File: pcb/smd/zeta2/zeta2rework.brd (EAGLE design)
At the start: 101.3 x 85.1 mm, 38 parts, among them IC1 MAX6520, IC2 L293DD, U2 INA219, U4 INA219

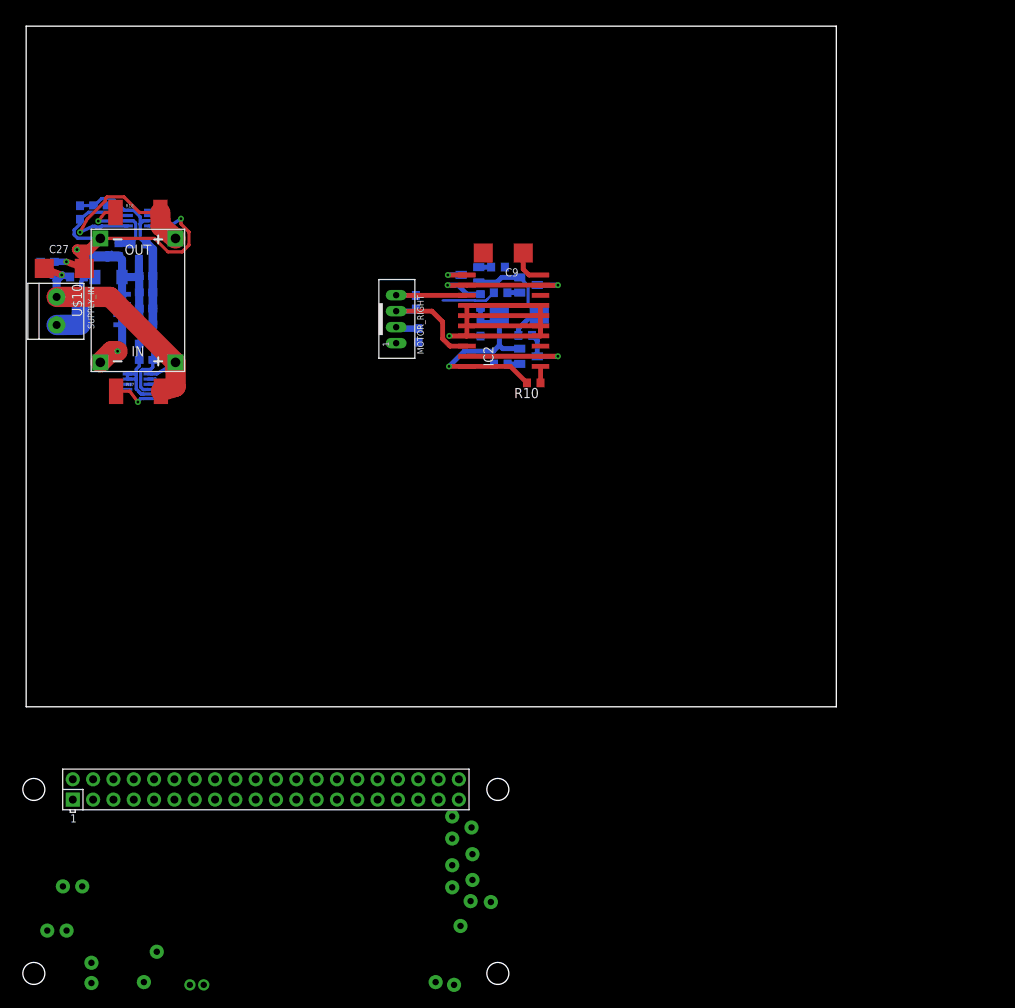
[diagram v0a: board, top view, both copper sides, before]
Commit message: added i2c device
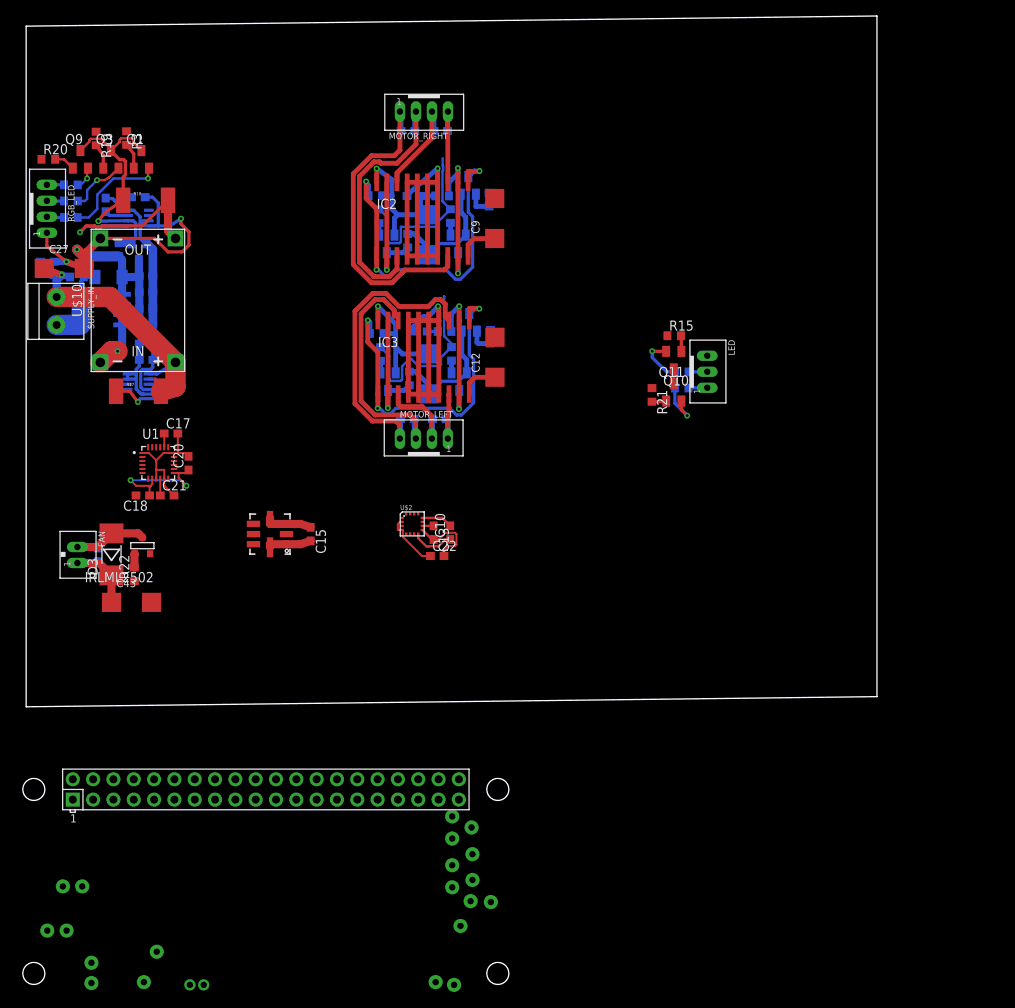
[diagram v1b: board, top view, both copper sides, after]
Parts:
- added C10: 0.22µF, rcl:C0603
- added C12, C43: 47µF, rcl:SMC_C
- added C13, C22: 4.7µF, rcl:C0603
- added C14: 100µF, rcl:SMC_C
- added C15: 100nF, rcl:C0603
- added C17: 2,2nF, rcl:C0603
- added C18, C20, C21: 0.1µF, rcl:C0603
- added C2: 0.1nF, rcl:C0603
- added C3, C31, C41: 10nF, rcl:C0603
- added D3: 1N4004 SMD, diode:MELF-MLL41
- added FAN: JST-PH_2-PIN_HEADER, srg:JST_B2B-PH_HEADER
- added IC3: L293DD, st-microelectronics:SO20
- added IRLML2502: (no value), zetex:SOT-23
- added LED: JST-PH_3-PIN_HEADER, srg:JST_B3B-PH_HEADER
- added MOTOR_LEFT, RGB_LED: JST-PH_4-PIN_HEADER, srg:JST_B4B-PH_HEADER
- added Q1, Q10, Q11, Q3, Q5, Q6, Q8, Q9: (no value), semicon-smd-ipc:SOT23
- added R12, R14, R8: 100k, rcl:R0603
- added R13, R5, R6: 500R, rcl:R0603
- added R15, R19, R20, R21, R3: 500, rcl:R0603
- added R16, R26, R27, R28, R4: 220R, rcl:R0603
- added R22: 22R, rcl:R0603
- added U$2: HMC5883L, HMC5883L:LPCC-16
- added U$3: BMP085, BMP085:BMP085
- added U1: MPU-6050, MPU-6050:QFN50P400X400X95-24N
- moved R10 30.7 mm to (43.6, 60.1), flipped to the bottom
- moved MOTOR_RIGHT 26.2 mm to (49.7, 70.6), turned to 180 degrees
- moved C28 25.6 mm to (47.7, 68.1), turned to 0 degrees
- moved R1 23.9 mm to (44.1, 57.5), turned to 270 degrees
- moved Q2 22.6 mm to (45.1, 54.1), turned to 180 degrees
- moved C29 21.6 mm to (51.8, 68.2), turned to 0 degrees
- moved R7 18.9 mm to (47.7, 54.5), turned to 270 degrees
- moved C1 18.6 mm to (48.5, 60.0), turned to 0 degrees
- moved IC2 16.3 mm to (49.5, 57.1), turned to 0 degrees
- moved C11 15.5 mm to (50.0, 55.2), turned to 270 degrees
- moved R9 14.0 mm to (52.0, 60.0), turned to 0 degrees
- moved R11 11.4 mm to (53.0, 57.5), turned to 270 degrees
- moved Q4 11.2 mm to (55.3, 61.4), turned to 0 degrees
- moved Q7 10.2 mm to (54.0, 54.1), turned to 180 degrees
- moved R2 8.51 mm to (57.9, 59.6), turned to 270 degrees
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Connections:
- new net BMP_EOC: U$3.2
- new net HMC_RDY: U$2.15
- new net MPU_INT: U1.12
- new net M_DIR_2: R13.1, R5.1
- new net N$13: Q5.1, R5.2
- new net N$14: Q6.1, R6.2
- new net N$15: Q8.1, R13.2
- new net N$16: R27.2, RGB_LED.P3
- new net N$19: R28.2, RGB_LED.P2
- new net N$2: C31.2, IC3.18, MOTOR_LEFT.P3
- new net N$22: Q1.1, R3.2
- new net N$23: Q3.1, R19.2
- new net N$24: Q1.2, R28.1
- new net N$25: C3.2, IC3.8, MOTOR_LEFT.P1
- new net N$26: C3.1, IC3.3, MOTOR_LEFT.P2
- new net N$27: Q10.1, R15.2
- new net N$28: Q3.2, R27.1
- new net N$29: Q9.2, R26.1
- new net N$3: C31.1, IC3.13, MOTOR_LEFT.P4
- new net N$30: Q10.2, R4.1
- new net N$31: Q11.1, R21.2
- new net N$32: Q9.1, R20.2
- new net N$33: Q11.2, R16.1
- new net N$34: C17.1, U1.20
- new net N$35: LED.P1, R16.2
- new net N$36: C21.1, U1.10
- new net N$37: IRLML2502.3, R22.2
- new net N$38: C10.2, U$2.12
- new net N$39: C10.1, U$2.8
- new net N$4: R26.2, RGB_LED.P4
- new net N$40: C13.1, U$2.10
- new net N$48: LED.P2, R4.2
- new net N$55: C41.2, D3.A, FAN.P2, IRLML2502.1
- new net N$6: IC3.12, IC3.9, Q8.3, R8.1
- new net N$7: IC3.19, IC3.2, Q5.3, R14.2
- new net N$9: IC3.1, IC3.11, Q6.3, R12.1
- new net PWM_FAN: R22.1
- new net PWM_M_EN_2: R6.1
- new net SCL1: U$2.1
- new net SDA1: U$2.16
- net +3V3: now also C15.1, C18.1, C20.1, C22.1, U$2.13, U$2.2, U$2.4, U$3.3, U$3.4, U1.13, U1.8
- net +5V: now also C14.+, C2.1, IC3.20, Q1.3, Q10.3, Q11.3, Q3.3, Q5.2, Q9.3, R12.2, R8.2
- net +8V: now also C12.+, C41.1, C43.+, D3.C, FAN.P1, IC3.10
- net GND: now also C12.-, C13.2, C14.-, C15.2, C17.2, C18.2, C2.2, C20.2, C21.2, C22.2, C43.-, IC3.14, IC3.15, IC3.16, IC3.17, IC3.4, IC3.5, IC3.6, IC3.7, IRLML2502.2, LED.P3, Q6.2, Q8.2, R14.1, RGB_LED.P1, U$2.11, U$2.9, U$3.1, U$3.8, U1.1, U1.11, U1.18, U1.9
- net SCL: now also U$3.6, U1.23
- net SDA: now also U$3.7, U1.24
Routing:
- net GND: track 153.1 -> 254.5 mm, vias 5 -> 6
- net N$9: track 0.00 -> 42.5 mm, vias 0 -> 3
- net N$3: track 0.00 -> 38.2 mm
- net N$20: track 2.62 -> 40.7 mm
- net N$8: track 6.10 -> 43.2 mm, vias 1 -> 3
- net N$21: track 0.17 -> 33.7 mm
- net +5V: track 40.3 -> 72.4 mm, vias 2 -> 3
- net N$2: track 0.00 -> 29.8 mm
- net +3V3: track 34.5 -> 62.6 mm, vias 0 -> 2
- net M_DIR_2: track 0.00 -> 23.0 mm
- net N$6: track 0.00 -> 18.7 mm, vias 0 -> 2
- net +8V: track 14.1 -> 30.6 mm
- net N$7: track 0.00 -> 16.1 mm, vias 0 -> 1
- net M_DIR_1: track 6.82 -> 22.4 mm
- net N$24: track 0.00 -> 13.2 mm, vias 0 -> 1
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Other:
- board size 101.3 x 85.1 mm -> 106.3 x 86.4 mm

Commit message: worked on pcb, fixed stm32 layout
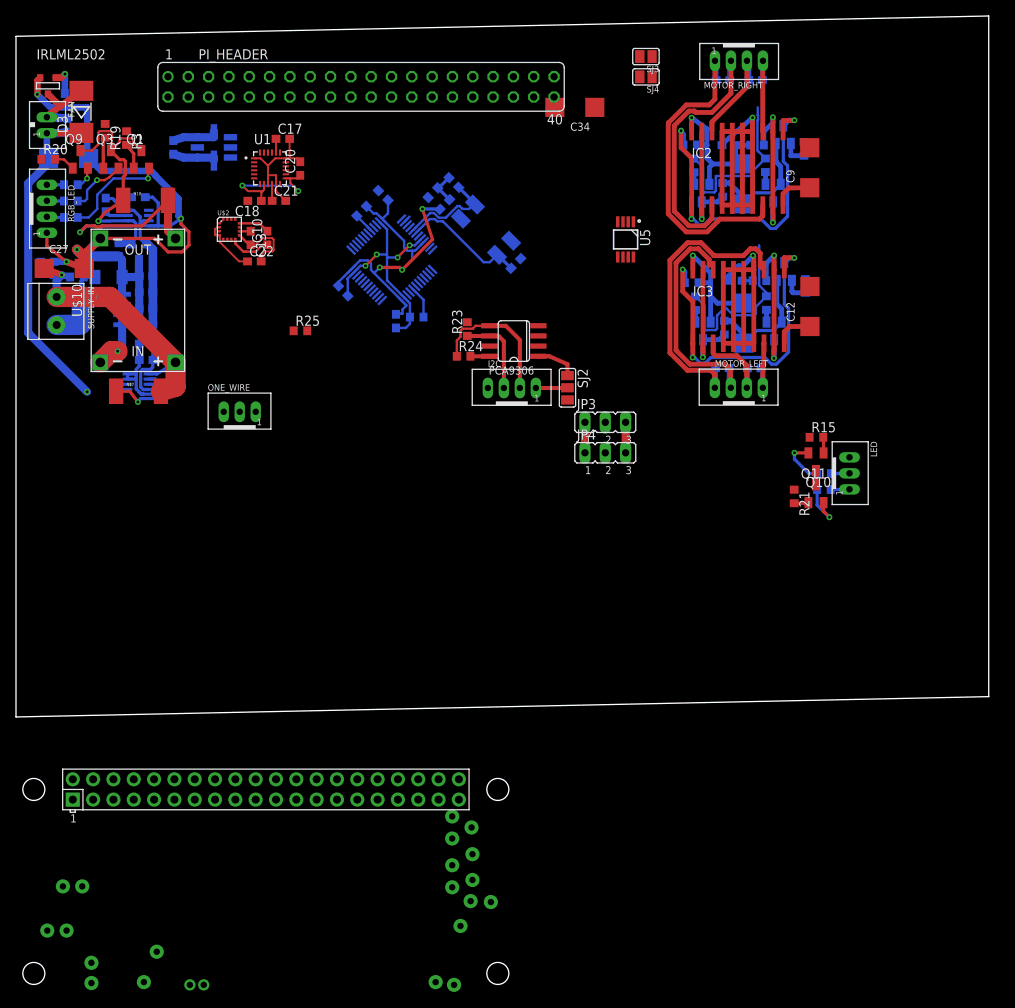
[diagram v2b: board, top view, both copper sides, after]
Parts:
- added C33, C38, C39, C40: 10nF, rcl:C0603
- added C34: 47µF, rcl:SMC_C
- added C36, C37: 10µF, rcl:C0603
- added I2C: JST-PH_4-PIN_HEADER, srg:JST_B4B-PH_HEADER
- added JP3, JP4: (no value), jumper:JP2
- added ONE_WIRE: JST-PH_3-PIN_HEADER, srg:JST_B3B-PH_HEADER
- added PCA9306: (no value), srg:SOIC-8
- added PI_HEADER: (no value), con-lsta:FE20-2
- added Q12: 8MHz, crystal-geyer_V1_0:7.0X5.0
- added R23, R24: 5k, rcl:R0603
- added R25: 4k7, rcl:R0603
- added R30, R31, R33: 100k, rcl:R0603
- added SJ2: (no value), jumper:SJ_2
- added SJ3, SJ4: (no value), microbuilder:SOLDERJUMPER_REFLOW_NOPASTE
- added U$4: STM32F103C8T6, STM32F103C8T6:LQFP48_7X7MM_0.5MMPP
- added U5: DS18B20U+, DS18B20U_:SOP65P490X95-8N
- moved R22 60.6 mm to (5.69, 72.8), flipped to the bottom, turned to 0 degrees
- moved IRLML2502 58.7 mm to (2.69, 73.8), turned to 0 degrees
- moved C43 56.1 mm to (5.31, 64.7), flipped to the bottom, turned to 180 degrees
- moved D3 55.4 mm to (6.91, 70.6)
- moved FAN 53.9 mm to (2.54, 69.0)
- moved C41 53.8 mm to (5.16, 68.9)
- moved C15 51.3 mm to (18.4, 66.1), flipped to the bottom
- moved U$3 48.8 mm to (23.5, 66.1), flipped to the bottom
- moved C10 43.3 mm to (30.1, 54.8)
- moved C13 43.3 mm to (28.1, 54.8)
- moved C22 43.3 mm to (28.5, 51.9)
- moved U$2 43.3 mm to (25.4, 55.9)
- moved C29 39.9 mm to (91.2, 74.5)
- moved R10 39.9 mm to (83.0, 66.4)
- moved C1 39.9 mm to (87.8, 66.4)
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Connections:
- new net ANALOG_3V3: U$4.10
- new net BOOT0: JP3.2, R31.2, U$4.44
- new net BOOT1: JP4.2, R33.1, U$4.20
- new net BOOT2: PI_HEADER.29
- new net BOOT3: PI_HEADER.27
- new net N$41: I2C.P1, PCA9306.7, PCA9306.8, R23.2, R24.2, SJ2.2
- new net N$42: I2C.P3, PCA9306.6, R23.1
- new net N$43: I2C.P2, PCA9306.5, R24.1
- new net N$44: PI_HEADER.37, SJ3.2
- new net N$45: PI_HEADER.35, SJ4.2
- new net N$46: C36.2, Q12.1, U$4.6
- new net N$47: C37.2, Q12.3, U$4.5
- new net N$49: R30.1, U$4.2
- new net NRST: PI_HEADER.26, U$4.7
- new net PIN_OUT: U$4.28
- new net SCL2: PCA9306.2
- new net SCL3: SJ4.1
- new net SDA2: PCA9306.3
- new net SDA3: SJ3.1
- new net SWCLK: PI_HEADER.20
- new net SWDCLK: U$4.37
- new net SWDIO: PI_HEADER.24, U$4.34
- new net S_DIR: U$4.14
- new net S_PWM_SPEED: U$4.19
- new net TEMPERATURE: ONE_WIRE.P2, R25.1, U5.1
- new net USART1_RX: U$4.31
- new net USART1_TX: U$4.30
- new net USART2_RX: PI_HEADER.34, U$4.13
- new net USART2_TX: PI_HEADER.32, U$4.12
- new net USB_DM: U$4.32
- new net USB_DP: U$4.33
- net +3V3: now also C33.1, C38.1, C39.1, C40.1, JP3.1, JP4.1, ONE_WIRE.P1, PCA9306.1, R25.2, R31.1, SJ2.1, U$4.24, U$4.36, U$4.48, U$4.9, U5.8
- net +5V: now also C34.+, PI_HEADER.38, PI_HEADER.40, SJ2.3
- net GND: now also C33.2, C34.-, C36.1, C37.1, C38.2, C39.2, C40.2, I2C.P4, JP3.3, JP4.3, ONE_WIRE.P3, PCA9306.4, PI_HEADER.1, PI_HEADER.12, PI_HEADER.15, PI_HEADER.22, PI_HEADER.28, PI_HEADER.31, PI_HEADER.36, PI_HEADER.8, R30.2, R33.2, U$4.23, U$4.35, U$4.47, U$4.8, U5.4
- net M_DIR_1: now also U$4.15, U$4.17
- net PWM_M_EN_1: now also U$4.16
- net PWM_M_EN_2: now also U$4.18
- net SCL: now also U$4.42
- net SDA: now also U$4.43
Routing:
- net GND: track 254.5 -> 323.8 mm, vias 6 -> 11
- net +3V3: track 62.6 -> 118.9 mm, vias 2 -> 5
- net +8V: track 30.6 -> 63.1 mm, vias 1 -> 2
- net N$43: track 0.00 -> 17.8 mm
- net N$46: track 0.00 -> 16.0 mm
- net N$47: track 0.00 -> 12.1 mm
- net N$42: track 0.00 -> 10.7 mm
- net N$41: track 0.00 -> 6.32 mm
- net BOOT1: track 0.00 -> 4.04 mm
- net +5V: track 72.4 -> 75.2 mm
- net BOOT0: track 0.00 -> 2.53 mm
- net N$37: track 1.73 -> 3.80 mm, vias 0 -> 1
- net N$55: track 11.7 -> 10.3 mm
- net N$49: track 0.00 -> 0.92 mm
- net N$23: track 3.16 -> 3.93 mm
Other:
- board size 106.3 x 86.4 mm -> 121.6 x 87.6 mm

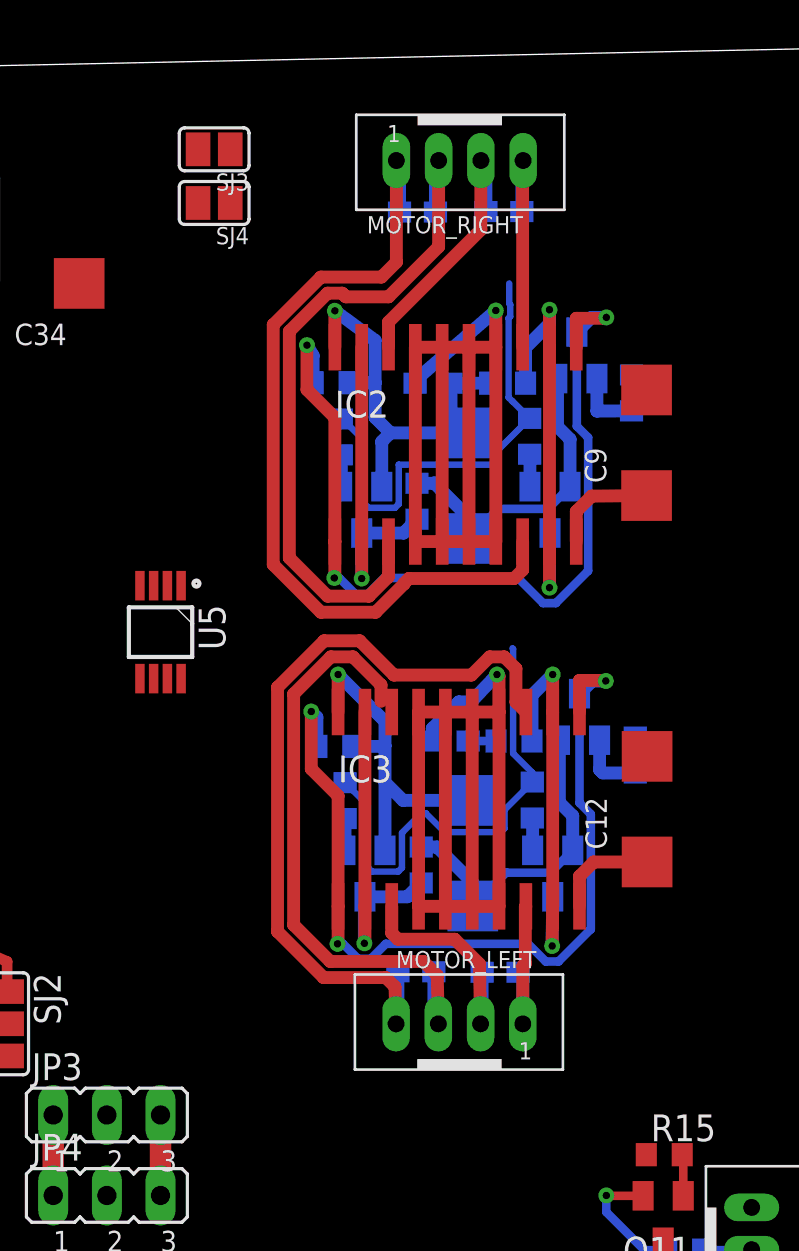
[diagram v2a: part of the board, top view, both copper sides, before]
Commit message: added temperature sensor to l239d, heatplate missing
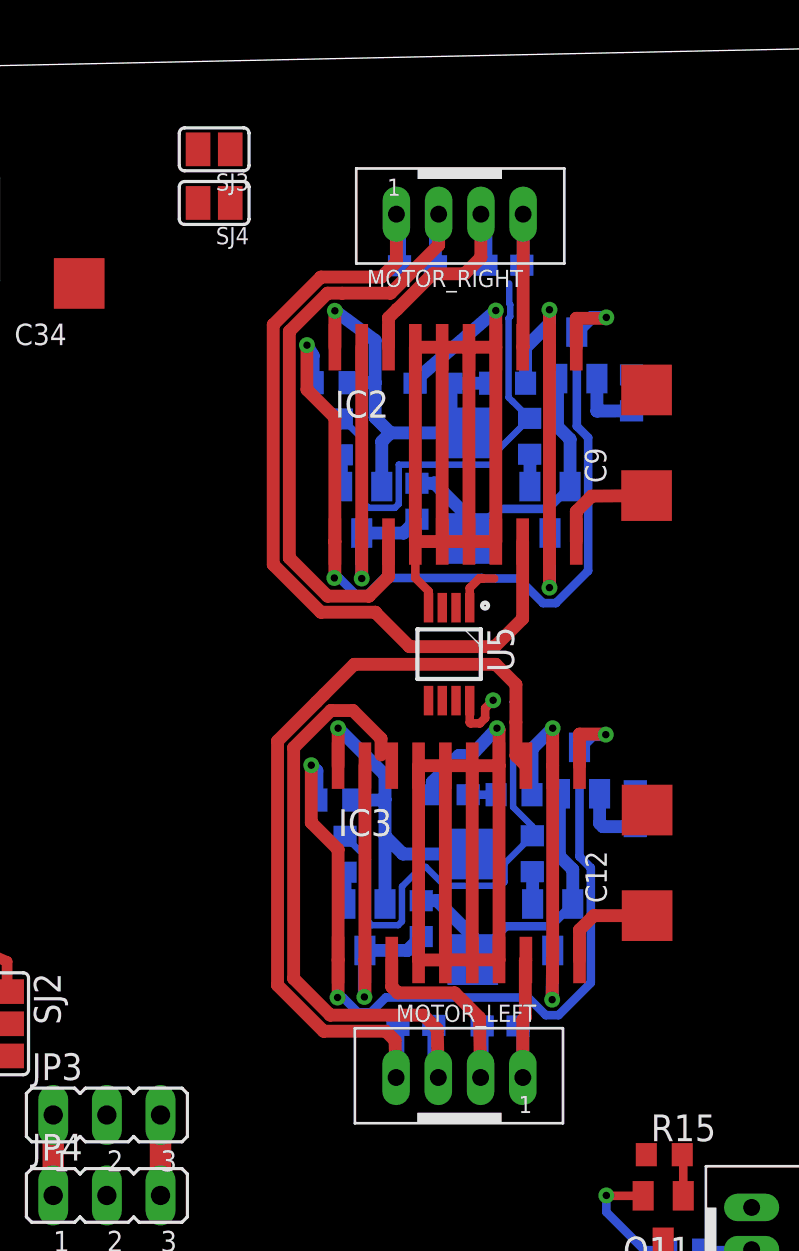
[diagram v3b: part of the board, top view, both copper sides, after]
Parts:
- moved U5 13.7 mm to (88.6, 53.6)
- moved C29 2.54 mm to (91.2, 72.0)
- moved R12 2.54 mm to (83.2, 46.7)
- moved C12 2.54 mm to (98.0, 43.7)
- moved C14 2.54 mm to (89.7, 41.6)
- moved C2 2.54 mm to (88.6, 46.9)
- moved C3 2.54 mm to (91.0, 36.0)
- moved C31 2.54 mm to (87.0, 36.0)
- moved IC3 2.54 mm to (89.1, 43.7)
- moved MOTOR_LEFT 2.54 mm to (89.1, 33.5)
- moved Q5 2.54 mm to (84.6, 40.6)
- moved Q6 2.54 mm to (94.8, 48.1)
- moved Q8 2.54 mm to (93.5, 40.6)
- moved R13 2.54 mm to (92.5, 44.1)
- moved R14 2.54 mm to (87.3, 41.0)
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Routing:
- net GND: track 323.8 -> 327.1 mm
- net +3V3: track 118.9 -> 121.7 mm, vias 5 -> 6
- net N$21: track 33.7 -> 30.9 mm
- net N$17: track 11.3 -> 8.75 mm
- net TEMPERATURE: track 0.00 -> 2.43 mm
- net N$18: track 13.2 -> 11.5 mm
- net N$3: track 38.2 -> 39.7 mm
